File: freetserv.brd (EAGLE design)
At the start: 91.4 x 82.5 mm, 80 parts, among them IC1 MCP16311-E/MS, IC2 SN75240PW, IC3 TUSB2046BVF, IC4 FT4232HL, IC5 MAX3232ECPW, IC6 MAX3232ECPW, IC7 MAX3232ECPW, IC8 MAX3232ECPW, Q1 12MHz, Q2 6MHz

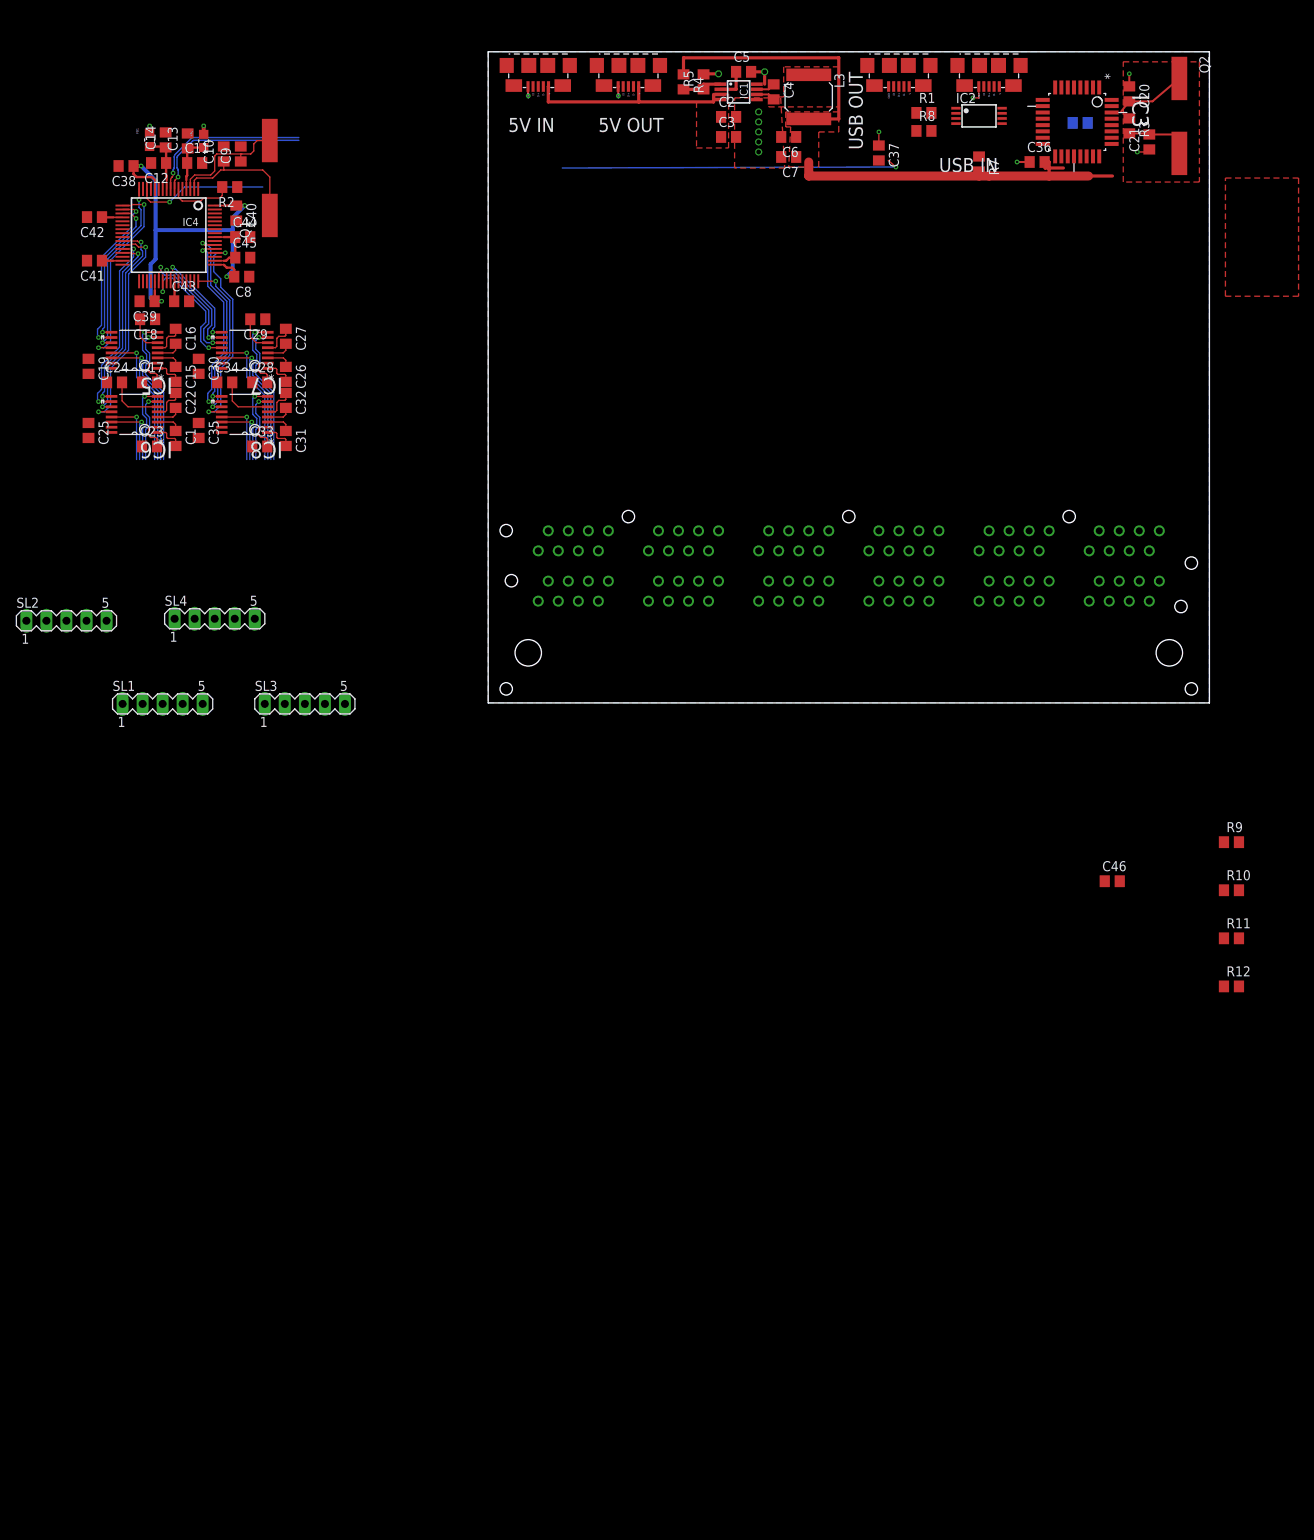
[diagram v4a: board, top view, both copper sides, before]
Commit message: Volker finished the FTDI routing, duplicated it
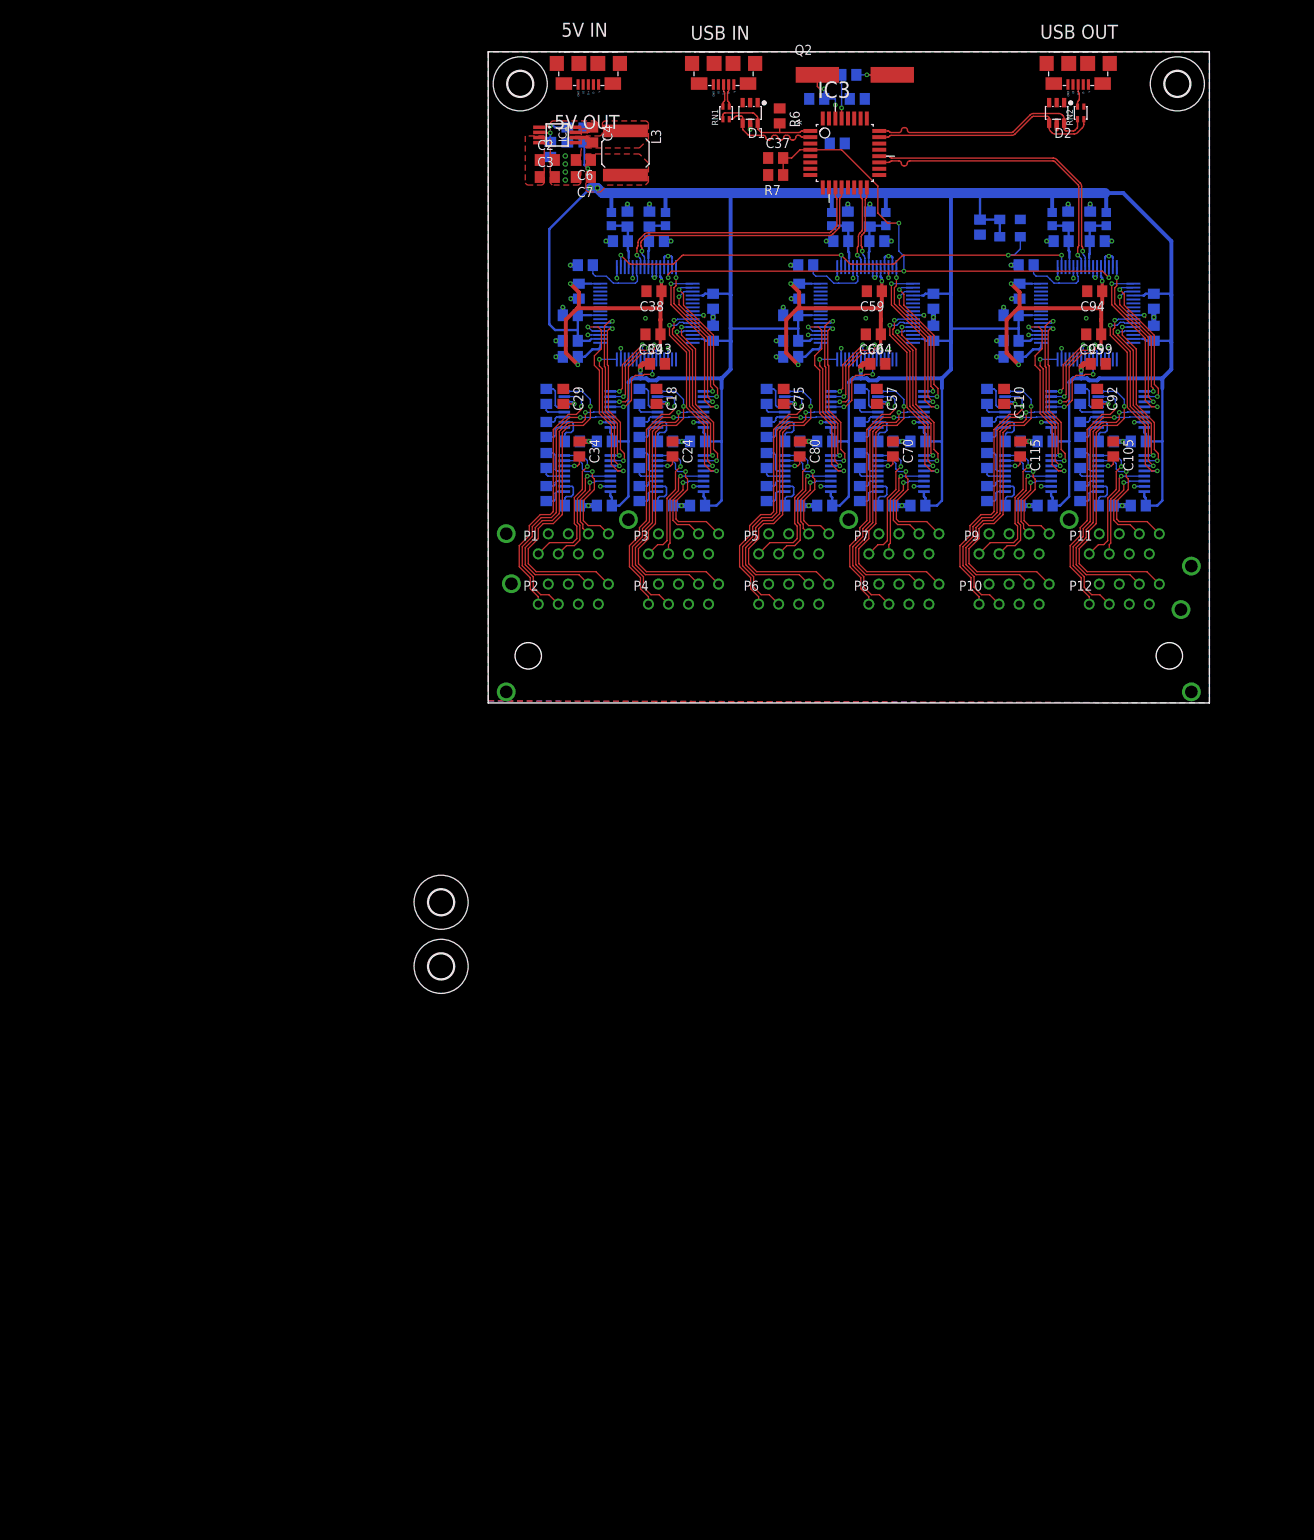
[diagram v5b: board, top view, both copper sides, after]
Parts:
- removed C10, C9: 18pF, resistor:C0805
- removed IC2: SN75240PW, sn65220_40:TSSOP8
- removed Q1: 12MHz, crystal:CSM-7X-DU
- removed R1, R10, R8, R9: 27, resistor:R0805
- removed R11, R12: 10k, resistor:R0805
- removed SL1, SL2, SL3, SL4: (no value), con-lstb:MA05-1
- removed USB_IN, USB_RASPI_DATA, USB_RASPI_DATA2: USB_MICROB, ftdi_ft231xq-r:USB_MICROB_PACKAGE
- added C100, C101, C102, C103, C104, C105, C106, C107, C108, C109, C110, C111, C112, C113, C114, C115, C116, C47, C489, C519, C54, C55, C56, C57, C58, C59, C60, C61, C62, C63, C64, C65, C66, C67, C68, C69, C70, C71, C72, C73, C74, C75, C76, C77, C78, C79, C80, C81, C859, C869, C89, C90, C91, C92, C93, C94, C95, C96, C97, C98, C99: 0.1uF, resistor:C0805
- added C502, C53, C879, C889: 4.7uF, resistor:C0805
- added C629, C829: 3.3uF, resistor:C0805
- added D1, D2: SN65220, texas1:SOT23-6
- added FB2, FB2\1, FB2\2, FB3: 330, Wurth_Elektronik_Passive_rev15d:WE-KI_0805A
- added H1, H2, H3, H4: MOUNT-HOLE3.2, holes:3,2
- added IC10, IC11, IC12, IC13, IC15, IC16, IC17, IC18: MAX3232ECPW, Texas Instruments_By_element14_Batch_1:SOP65P640X120-16N
- added IC14, IC9: FT4232HL, ftdichip-6:LQFP64
- added QG1: ASV-12.000MHZ-EJ-T, crystal:XO53
- added R13, R15: 12K / 1%, resistor:R0805
- added RN1, RN2: 27, resistor-net:EXBV4V
- added USB_HOST, USB_OUT: USB_MICROB, ftdi_ft231xq-r:USB_MICROB_PACKAGE
- moved C46 99.8 mm to (44.3, 70.9), flipped to the bottom
- moved C42 79.1 mm to (28.5, 50.9), flipped to the bottom, turned to 270 degrees
- moved C41 79.0 mm to (28.5, 46.9), flipped to the bottom, turned to 90 degrees
- moved C19 77.8 mm to (26.5, 33.1), flipped to the bottom, turned to 180 degrees
- moved C25 77.8 mm to (26.5, 25.0), flipped to the bottom, turned to 180 degrees
- moved C24 71.2 mm to (23.4, 32.2), turned to 270 degrees
- moved IC5 69.6 mm to (24.4, 37.2), flipped to the bottom
- moved IC6 69.6 mm to (24.4, 29.1), flipped to the bottom
- moved C38 68.8 mm to (21.0, 52.2)
- moved FB1 66.2 mm to (22.5, 61.3), flipped to the bottom
- moved C17 65.8 mm to (22.5, 33.1), flipped to the bottom
- moved C23 65.8 mm to (22.5, 25.0), flipped to the bottom
- moved C18 65.3 mm to (21.3, 38.9), turned to 270 degrees
- moved C39 64.3 mm to (20.9, 46.7)
- moved C12 63.9 mm to (21.3, 58.5), flipped to the bottom
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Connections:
- net +1V8 renamed +1V8-1
- removed net !OVRCUR1: IC3.10, R11.2
- removed net !OVRCUR2: IC3.14, R12.2
- removed net !OVRCUR3: IC3.18
- removed net !OVRCUR4: IC3.22
- removed net !PWRON1: IC3.9
- removed net !PWRON2: IC3.13
- removed net !PWRON3: IC3.17
- removed net !PWRON4: IC3.21
- removed net DX1_N: R9.1, USB_IN.D-
- removed net N$15: C9.1, IC4.3, Q1.2
- removed net N$16: C10.1, IC4.2, Q1.1
- new net +1V8-2: C59.1, C60.1, C61.1, C629.2, IC9.12, IC9.37, IC9.49, IC9.64
- new net +1V8-3: C829.2, C94.1, C95.1, C96.1, IC14.12, IC14.37, IC14.49, IC14.64
- new net 12MHZ: IC14.2, IC4.2, IC9.2, QG1.3
- new net CTS1E1: IC10.8, U$1.P8.8
- new net CTS1E2: IC15.8, U$1.P12.8
- new net CTS1I1: IC10.9, IC9.19
- new net CTS1I2: IC14.19, IC15.9
- new net CTS2E1: IC11.8, U$1.P7.8
- new net CTS2E2: IC16.8, U$1.P11.8
- new net CTS2I1: IC11.9, IC9.29
- new net CTS2I2: IC14.29, IC16.9
- new net CTS3E1: IC12.8, U$1.P6.8
- new net CTS3E2: IC17.8, U$1.P10.8
- new net CTS3I1: IC12.9, IC9.41
- new net CTS3I2: IC14.41, IC17.9
- new net CTS4E1: IC13.8, U$1.P5.8
- new net CTS4E2: IC18.8, U$1.P9.8
- new net CTS4I1: IC13.9, IC9.54
- new net CTS4I2: IC14.54, IC18.9
- new net N$100: C103.2, IC16.4
- new net N$101: C103.1, IC16.5
- new net N$102: C104.2, IC16.2
- new net N$103: C105.2, IC16.6
- new net N$104: C107.2, IC17.1
- new net N$105: C107.1, IC17.3
- new net N$106: C108.2, IC17.4
- new net N$107: C108.1, IC17.5
- new net N$108: C109.2, IC17.2
- new net N$109: C110.2, IC17.6
- new net N$110: C112.2, IC18.1
- new net N$111: C112.1, IC18.3
- new net N$112: C113.2, IC18.4
- new net N$113: C113.1, IC18.5
- new net N$114: C114.2, IC18.2
- new net N$115: C115.2, IC18.6
- new net N$1355: C519.1, C53.1, FB2.2, IC9.9
- new net N$19: C54.2, IC10.1
- new net N$20: C54.1, IC10.3
- new net N$23: C55.2, IC10.4
- new net N$24: C55.1, IC10.5
- new net N$25: C56.2, IC10.2
- new net N$26: C57.2, IC10.6
- new net N$27: C67.2, IC11.1
- new net N$28: C67.1, IC11.3
- new net N$29: C68.2, IC11.4
- new net N$30: C68.1, IC11.5
- new net N$35: C69.2, IC11.2
- new net N$36: C70.2, IC11.6
- new net N$38: C72.2, IC12.1
- new net N$41: C72.1, IC12.3
- new net N$42: C73.2, IC12.4
- new net N$43: C73.1, IC12.5
- new net N$5: IC9.6, R13.2
- new net N$50: C74.2, IC12.2
- new net N$51: C75.2, IC12.6
- new net N$5499: C77.2, IC13.1
- new net N$55: C77.1, IC13.3
- new net N$555: C489.1, C502.1, FB2\1.2, IC9.4
- new net N$56: C78.2, IC13.4
- new net N$57: C78.1, IC13.5
- new net N$58: C79.2, IC13.2
- new net N$59: C80.2, IC13.6
- new net N$64: IC14.6, R15.2
- new net N$69: C859.1, C879.1, FB2\2.2, IC14.4
- new net N$7: RN2.B2, USB_OUT.D-
- new net N$70: C869.1, C889.1, FB3.2, IC14.9
- new net N$71: C89.2, IC15.1
- new net N$72: C89.1, IC15.3
- new net N$73: C90.2, IC15.4
- new net N$74: C90.1, IC15.5
- new net N$75: C91.2, IC15.2
- new net N$76: C92.2, IC15.6
- new net N$98: C102.2, IC16.1
- new net N$99: C102.1, IC16.3
- new net RTS1E1: IC10.7, U$1.P8.1
- new net RTS1E2: IC15.7, U$1.P12.1
- new net RTS1I1: IC10.10, IC9.18
- new net RTS1I2: IC14.18, IC15.10
- new net RTS2E1: IC11.7, U$1.P7.1
- new net RTS2E2: IC16.7, U$1.P11.1
- new net RTS2I1: IC11.10, IC9.28
- new net RTS2I2: IC14.28, IC16.10
- new net RTS3E1: IC12.7, U$1.P6.1
- new net RTS3E2: IC17.7, U$1.P10.1
- new net RTS3I1: IC12.10, IC9.40
- new net RTS3I2: IC14.40, IC17.10
- new net RTS4E1: IC13.7, U$1.P5.1
- new net RTS4E2: IC18.7, U$1.P9.1
- new net RTS4I1: IC13.10, IC9.53
- new net RTS4I2: IC14.53, IC18.10
- new net RXD1E1: IC10.13, U$1.P8.6
- new net RXD1E2: IC15.13, U$1.P12.6
- new net RXD1I1: IC10.12, IC9.17
- new net RXD1I2: IC14.17, IC15.12
- new net RXD2E1: IC11.13, U$1.P7.6
- new net RXD2E2: IC16.13, U$1.P11.6
- new net RXD2I1: IC11.12, IC9.27
- new net RXD2I2: IC14.27, IC16.12
- new net RXD3E1: IC12.13, U$1.P6.6
- new net RXD3E2: IC17.13, U$1.P10.6
- new net RXD3I1: IC12.12, IC9.39
- new net RXD3I2: IC14.39, IC17.12
- new net RXD4E1: IC13.13, U$1.P5.6
- new net RXD4E2: IC18.13, U$1.P9.6
- new net RXD4I1: IC13.12, IC9.52
- new net RXD4I2: IC14.52, IC18.12
- new net TXD1E1: IC10.14, U$1.P8.3
- new net TXD1E2: IC15.14, U$1.P12.3
- new net TXD1I1: IC10.11, IC9.16
- new net TXD1I2: IC14.16, IC15.11
- new net TXD2E1: IC11.14, U$1.P7.3
- new net TXD2E2: IC16.14, U$1.P11.3
- new net TXD2I1: IC11.11, IC9.26
- new net TXD2I2: IC14.26, IC16.11
- new net TXD3E1: IC12.14, U$1.P6.3
- new net TXD3E2: IC17.14, U$1.P10.3
- new net TXD3I1: IC12.11, IC9.38
- new net TXD3I2: IC14.38, IC17.11
- new net TXD4E1: IC13.14, U$1.P5.3
- new net TXD4E2: IC18.14, U$1.P9.3
- new net TXD4I1: IC13.11, IC9.48
- new net TXD4I2: IC14.48, IC18.11
- net !RESET: now also IC14.14, IC9.14
- net +3V3: now also C100.1, C101.1, C106.2, C111.2, C116.2, C47.2, C58.2, C62.1, C63.1, C64.1, C65.1, C66.1, C71.2, C76.2, C81.2, C93.2, C97.1, C98.1, C99.1, FB2.1, FB2\1.1, FB2\2.1, FB3.1, IC10.16, IC11.16, IC12.16, IC13.16, IC14.20, IC14.31, IC14.42, IC14.50, IC14.56, IC15.16, IC16.16, IC17.16, IC18.16, IC3.10, IC3.14, IC3.18, IC3.22, IC9.20, IC9.31, IC9.42, IC9.50, IC9.56, QG1.1, QG1.4; no longer R11.1, R12.1
- net +5V: no longer USB_RASPI_DATA2.V
- net CTS1E: now also U$1.P4.8; no longer SL1.3
- net CTS2E: now also U$1.P3.8; no longer SL2.3
- net CTS3E: now also U$1.P2.8; no longer SL3.3
- net CTS4E: now also U$1.P1.8; no longer SL4.3
- net D0_N: now also D1.4, RN1.B1; no longer IC2.6, R1.2
- net D0_P: now also D1.6, RN1.A1; no longer IC2.8, R8.2
- net D1_N: now also D2.4, IC3.23, RN2.B1; no longer IC2.4, IC3.11, R9.2
- net D1_P: now also D2.6, IC3.24, RN2.A1; no longer IC2.2, IC3.12, R10.2
- net D2_N: now also IC3.11; no longer IC3.15
- net D2_P: now also IC3.12; no longer IC3.16
- net D3_N: now also IC3.15, IC9.7; no longer IC3.19
- net D3_P: now also IC3.16, IC9.8; no longer IC3.20
- net D4_N: now also IC14.7, IC3.19; no longer IC3.23
- net D4_P: now also IC14.8, IC3.20; no longer IC3.24
- net DX0_N: now also RN1.B2, USB_HOST.D-; no longer R1.1, USB_RASPI_DATA.D-
- net DX0_P: now also RN1.A2, USB_HOST.D+; no longer R8.1, USB_RASPI_DATA.D+
- net DX1_P: now also RN2.A2, USB_OUT.D+; no longer R10.1, USB_IN.D+
- net GND: now also C100.2, C101.2, C104.1, C105.1, C106.1, C109.1, C110.1, C111.1, C114.1, C115.1, C116.1, C47.1, C489.2, C502.2, C519.2, C53.2, C56.1, C57.1, C58.1, C59.2, C60.2, C61.2, C62.2, C629.1, C63.2, C64.2, C65.2, C66.2, C69.1, C70.1, C71.1, C74.1, C75.1, C76.1, C79.1, C80.1, C81.1, C829.1, C859.2, C869.2, C879.2, C889.2, C91.1, C92.1, C93.1, C94.2, C95.2, C96.2, C97.2, C98.2, C99.2, D1.2, D1.5, D2.2, D2.5, IC10.15, IC11.15, IC12.15, IC13.15, IC14.1, IC14.10, IC14.11, IC14.13, IC14.15, IC14.25, IC14.35, IC14.47, IC14.5, IC14.51, IC15.15, IC16.15, IC17.15, IC18.15, IC9.1, IC9.10, IC9.11, IC9.13, IC9.15, IC9.25, IC9.35, IC9.47, IC9.5, IC9.51, QG1.2, R13.1, R15.1, U$1.P1.4, U$1.P1.5, U$1.P10.4, U$1.P10.5, U$1.P11.4, U$1.P11.5, U$1.P12.4, U$1.P12.5, U$1.P2.4, U$1.P2.5, U$1.P3.4, U$1.P3.5, U$1.P4.4, U$1.P4.5, U$1.P5.4, U$1.P5.5, U$1.P6.4, U$1.P6.5, U$1.P7.4, U$1.P7.5, U$1.P8.4, U$1.P8.5, U$1.P9.4, U$1.P9.5, USB_HOST.GND, USB_OUT.GND; no longer C10.2, C9.2, IC2.1, IC2.3, IC2.5, IC2.7, SL1.5, SL2.5, SL3.5, SL4.5, USB_IN.GND, USB_RASPI_DATA.GND, USB_RASPI_DATA2.GND
- net RTS1E: now also U$1.P4.1; no longer SL1.4
- net RTS2E: now also U$1.P3.1; no longer SL2.4
- net RTS3E: now also U$1.P2.1; no longer SL3.4
- net RTS4E: now also U$1.P1.1; no longer SL4.4
- net RXD1E: now also U$1.P4.6; no longer SL1.1
- net RXD2E: now also U$1.P3.6; no longer SL2.1
- net RXD3E: now also U$1.P2.6; no longer SL3.1
- net RXD4E: now also U$1.P1.6; no longer SL4.1
- net TXD1E: now also U$1.P4.3; no longer SL1.2
- net TXD2E: now also U$1.P3.3; no longer SL2.2
- net TXD3E: now also U$1.P2.3; no longer SL3.2
- net TXD4E: now also U$1.P1.3; no longer SL4.2
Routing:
- net +3V3: track 97.7 -> 457.7 mm, vias 2 -> 6
- net GND: track 16.6 -> 124.0 mm, vias 14 -> 86
- net 12MHZ: track 0.00 -> 65.6 mm, vias 0 -> 4
- net +1V8-3: track 0.00 -> 43.1 mm, vias 0 -> 4
- net +1V8-2: track 0.00 -> 43.1 mm, vias 0 -> 4
- net CTS3E2: track 0.00 -> 40.8 mm, vias 0 -> 1
- net CTS3E1: track 0.00 -> 40.8 mm, vias 0 -> 1
- net CTS1E1: track 0.00 -> 39.2 mm, vias 0 -> 1
- net CTS1E2: track 0.00 -> 39.2 mm, vias 0 -> 1
- net D4_N: track 0.00 -> 37.7 mm, vias 0 -> 1
- net D4_P: track 0.00 -> 37.6 mm, vias 0 -> 1
- net RXD3E2: track 0.00 -> 36.5 mm, vias 0 -> 1
- net RXD3E1: track 0.00 -> 36.5 mm, vias 0 -> 1
- net RXD1E1: track 0.00 -> 34.8 mm, vias 0 -> 1
- net RXD1E2: track 0.00 -> 34.8 mm, vias 0 -> 1
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
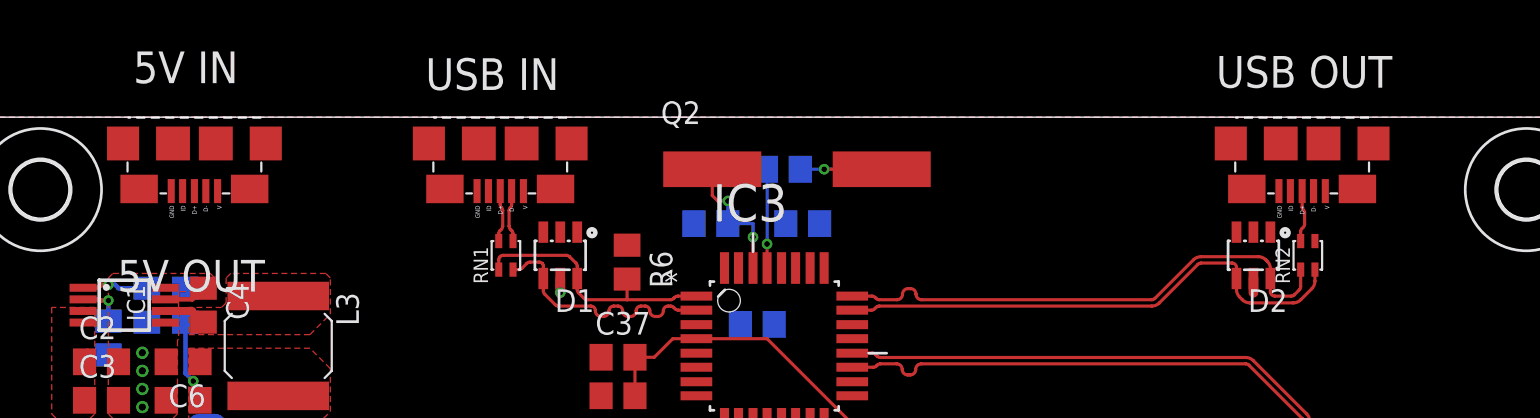
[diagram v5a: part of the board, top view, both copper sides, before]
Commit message: replace micro-USB power input with 2-pin header
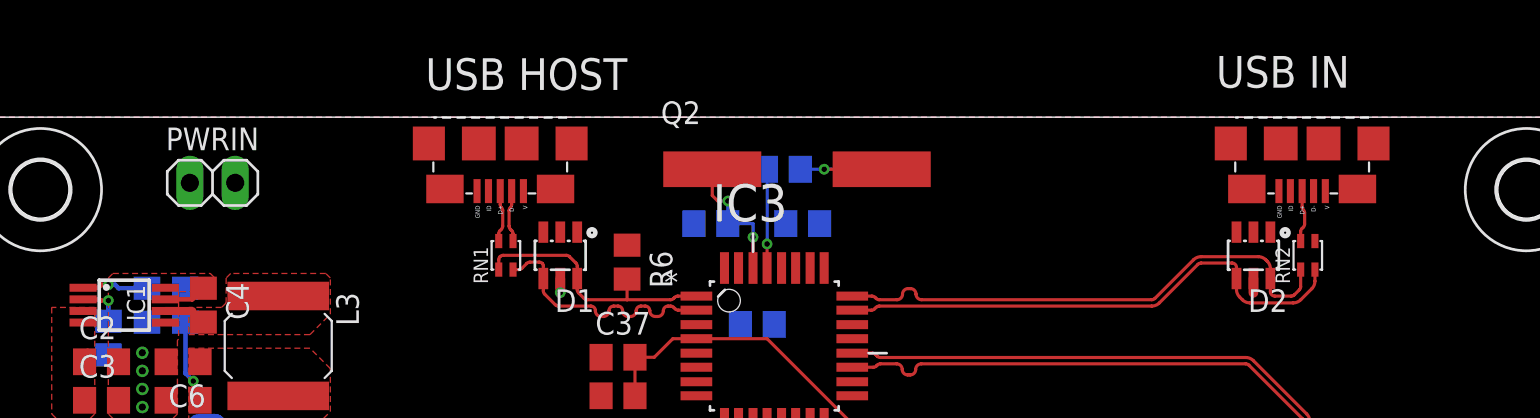
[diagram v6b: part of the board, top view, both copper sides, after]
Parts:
- removed USB_RASPI_PWR: USB_MICROB, ftdi_ft231xq-r:USB_MICROB_PACKAGE
- added PWRIN: (no value), pinhead:1X02
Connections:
- net +5V: now also PWRIN.1; no longer USB_RASPI_PWR.V
- net GND: now also PWRIN.2; no longer USB_RASPI_PWR.GND
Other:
- board text added: "USB HOST"
- board text removed: "5V IN"
- board text removed: "5V OUT"
- board text removed: "USB OUT"
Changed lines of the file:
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@@
 <?xml version="1.0" encoding="utf-8"?>
 <!DOCTYPE eagle SYSTEM "eagle.dtd">
-<eagle version="7.4.0">
+<eagle version="7.3.0">
 <drawing>
 <settings>
@@
 <wire x1="91.44" y1="82.55" x2="0" y2="82.55" width="0" layer="20"/>
 <wire x1="0" y1="82.55" x2="0" y2="0" width="0" layer="20"/>
-<text x="9.271" y="84.455" size="1.778" layer="21">5V IN</text>
-<text x="8.382" y="72.771" size="1.778" layer="21">5V OUT</text>
-<text x="69.977" y="84.201" size="1.778" layer="21">USB OUT</text>
-<text x="25.654" y="84.074" size="1.778" layer="21">USB IN</text>
+<text x="69.977" y="84.201" size="1.778" layer="21">USB IN</text>
+<text x="25.654" y="84.074" size="1.778" layer="21">USB HOST</text>
 </plain>
 <attributes>
@@
 <attribute name="PARTNO" value="H11634CT-ND" x="29.845" y="77.724" size="1.778" layer="27" rot="R180" display="off"/>
 </element>
-<element name="USB_RASPI_PWR" library="ftdi_ft231xq-r" package="USB_MICROB_PACKAGE" value="USB_MICROB" x="12.7" y="77.724" rot="R180">
-<attribute name="PARTNO" value="H11634CT-ND" x="12.7" y="77.724" size="1.778" layer="27" rot="R180" display="off"/>
-</element>
 <element name="IC5" library="Texas Instruments_By_element14_Batch_1" package="SOP65P640X120-16N" value="MAX3232ECPW" x="24.384" y="37.211" rot="MR180">
 <attribute name="PACKAGE" value="TSSOP-16" x="24.384" y="37.211" size="1.778" layer="28" rot="MR180" display="off"/>
@@
 <attribute name="PARTNO" value="1276-1003-1-ND" x="62.357" y="60.325" size="1.778" layer="28" rot="MR90" display="off"/>
 </element>
+<element name="PWRIN" library="pinhead" package="1X02" value="" x="13.716" y="78.867"/>
 </elements>
 <signals>
@@
 <contactref element="C20" pad="1"/>
 <contactref element="C21" pad="1"/>
-<contactref element="USB_RASPI_PWR" pad="GND"/>
 <contactref element="C3" pad="2"/>
 <contactref element="R5" pad="2"/>
@@
 <contactref element="C47" pad="1"/>
 <contactref element="QG1" pad="2"/>
+<contactref element="PWRIN" pad="2"/>
 <wire x1="72.0725" y1="76.103" x2="73.503" y2="78.404" width="0" layer="19" extent="1-1"/>
 <wire x1="72.0725" y1="73.503" x2="72.0725" y2="76.103" width="0" layer="19" extent="1-1"/>
@@
 <wire x1="11.067" y1="71.034" x2="10.033" y2="71.059" width="0" layer="19" extent="1-16"/>
 <wire x1="11.067" y1="72.984" x2="11.067" y2="71.034" width="0" layer="19" extent="1-1"/>
-<wire x1="11.4" y1="78.404" x2="11.067" y2="72.984" width="0" layer="19" extent="1-1"/>
+<wire x1="14.986" y1="78.867" x2="11.43" y2="12.5222" width="0" layer="19" extent="1-1"/>
 </signal>
 <signal name="+1V8-1">
@@
 <contactref element="C3" pad="1"/>
 <contactref element="C2" pad="1"/>
-<contactref element="USB_RASPI_PWR" pad="V"/>
 <contactref element="IC1" pad="4"/>
 <wire x1="6.543" y1="68.834" x2="6.713" y2="69.469" width="0.254" layer="1"/>
@@
 </polygon>
 <contactref element="IC1" pad="3"/>
-<wire x1="6.459" y1="71.684" x2="14" y2="78.404" width="0" layer="19" extent="1-1"/>
+<contactref element="PWRIN" pad="1"/>
 <wire x1="6.459" y1="71.034" x2="6.459" y2="71.684" width="0" layer="19" extent="1-1"/>
 <wire x1="6.713" y1="69.469" x2="6.459" y2="71.034" width="0" layer="19" extent="1-1"/>
 <wire x1="6.543" y1="66.675" x2="6.543" y2="68.834" width="0" layer="19" extent="1-1"/>
+<wire x1="12.446" y1="78.867" x2="6.543" y2="66.675" width="0" layer="19" extent="1-1"/>
 </signal>
 <signal name="N$3">
